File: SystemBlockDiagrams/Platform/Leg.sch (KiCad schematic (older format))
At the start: 15 parts

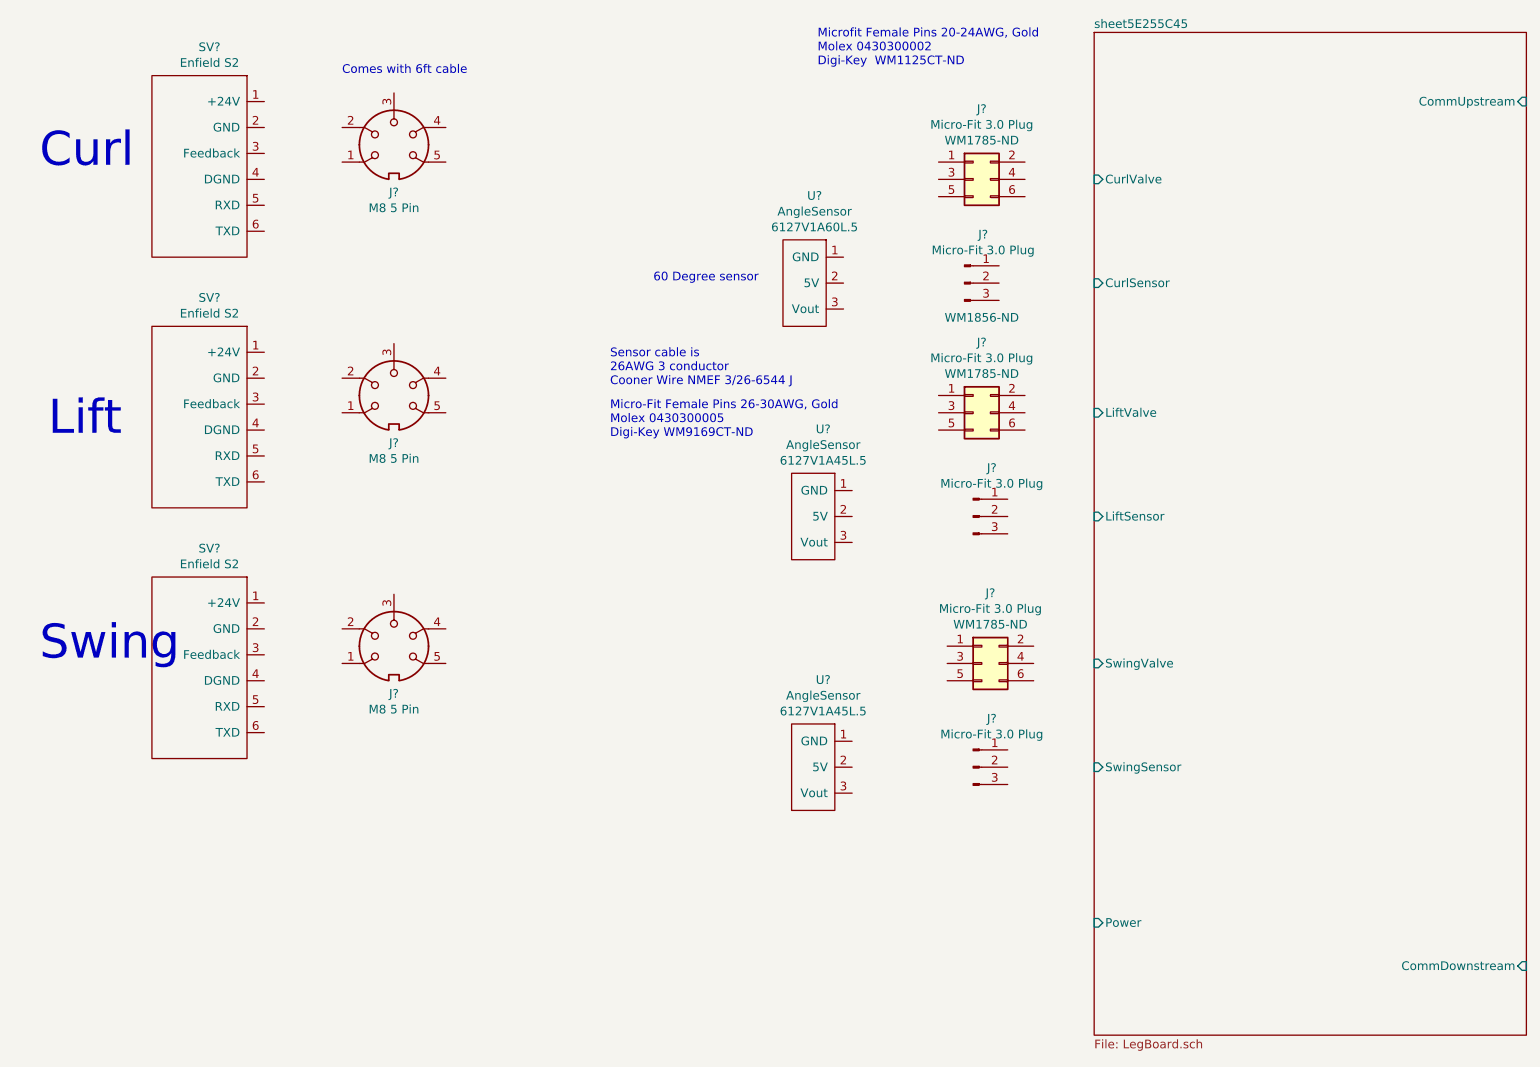
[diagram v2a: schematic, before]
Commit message: Update part numbers for BOM generation
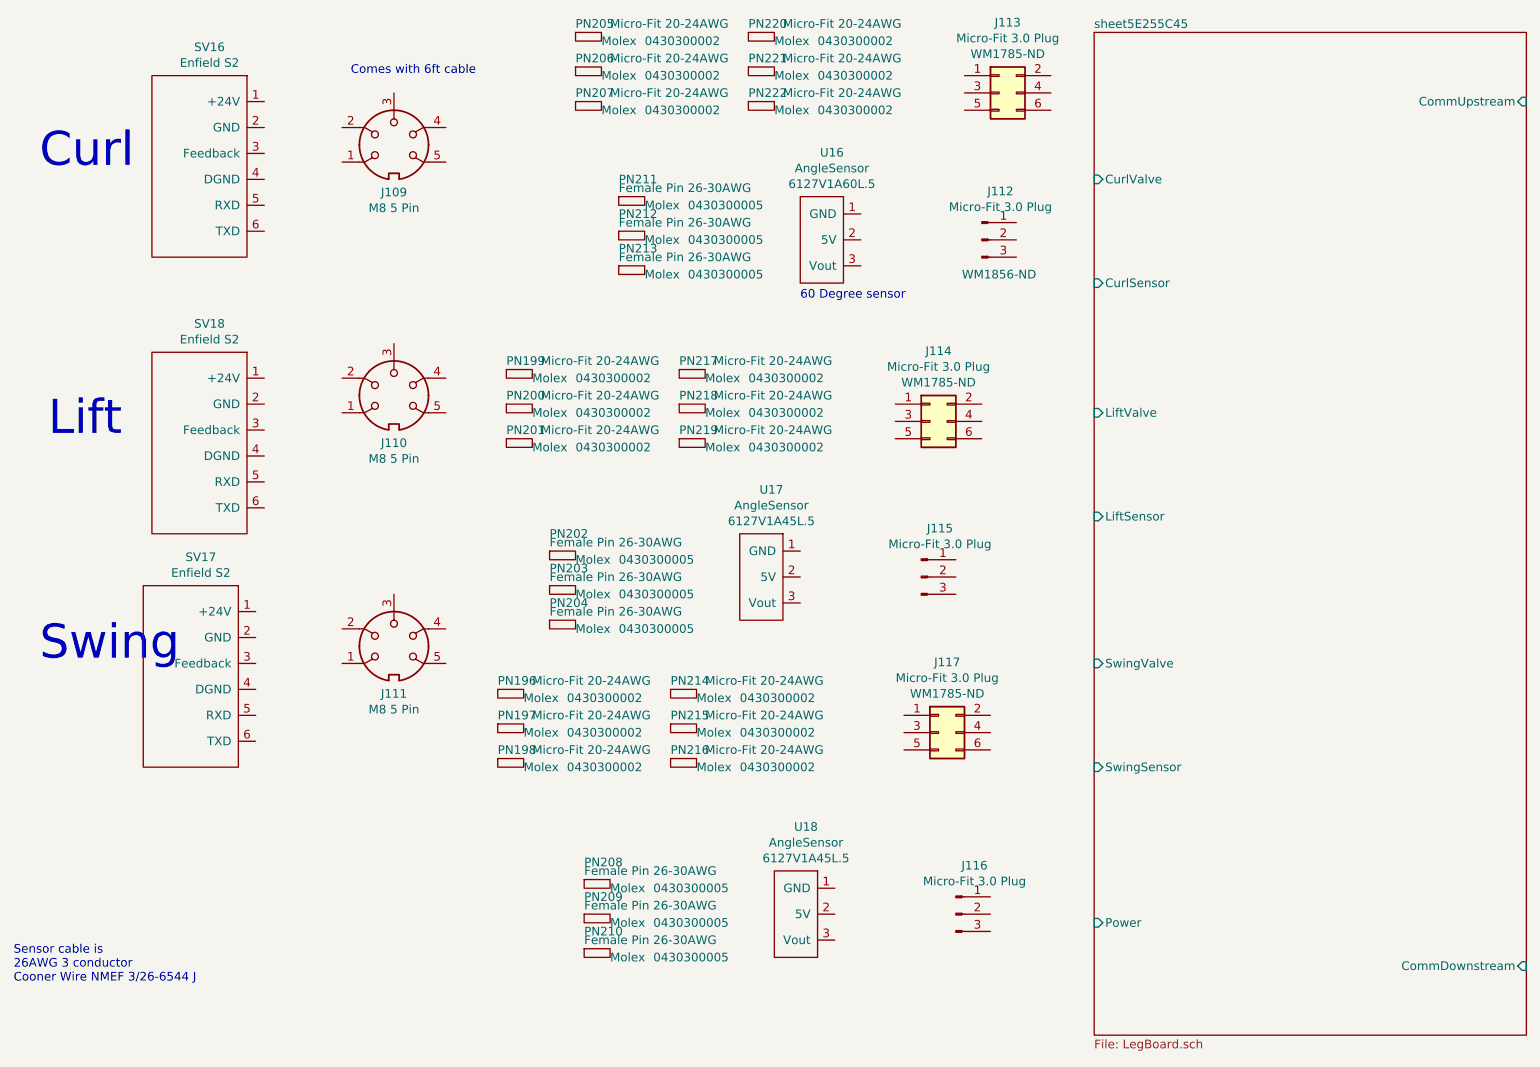
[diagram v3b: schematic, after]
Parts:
- removed SV? (x2): Enfield S2, symbol Stomp:PneumaticServoValve
- added PN142, PN143, PN144, PN145, PN146, PN147, PN151, PN152, PN153, PN160, PN161, PN162, PN163, PN164, PN165, PN166, PN167, PN168: Micro-Fit 20-24AWG, symbol Stomp:PIN
- added PN67, PN68, PN69, PN73, PN74, PN75, PN76, PN77, PN78: Female Pin 26-30AWG, symbol Stomp:PIN
- added SV2, SV3: Enfield S2, symbol Stomp:PneumaticServoValve
- J22, J25, J26: renamed from J?; Manufacturer (none) -> Molex; Manufcturer Molex -> (none); Suplier Digi-Key -> (none); Supplier (none) -> Digi-Key
- SV1: renamed from SV?; Manufacturer (none) -> Enfield; Manufacturer Part Number (none) -> S2; Supplier (none) -> Enfield; Supplier Part Number (none) -> S2
- gave numbers to parts that had none: 9
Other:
- note removed: "Micro-Fit Female Pins 26-30AWG, Gold\nMolex 0430300005\nDigi-Key WM9169CT-ND"
- note removed: "Microfit Female Pins 20-24AWG, Gold\nMolex 0430300002\nDigi-Key WM1125CT-ND"
- moved on the sheet: J112, J113, J114, J115, J116, J117, U16, U17, U18
